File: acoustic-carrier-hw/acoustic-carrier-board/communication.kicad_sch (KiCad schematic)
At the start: 46 parts, among them IC1 ECP5-BGA256, J9 HR911130A, U1 KSZ9031RN, Y1 25MHz

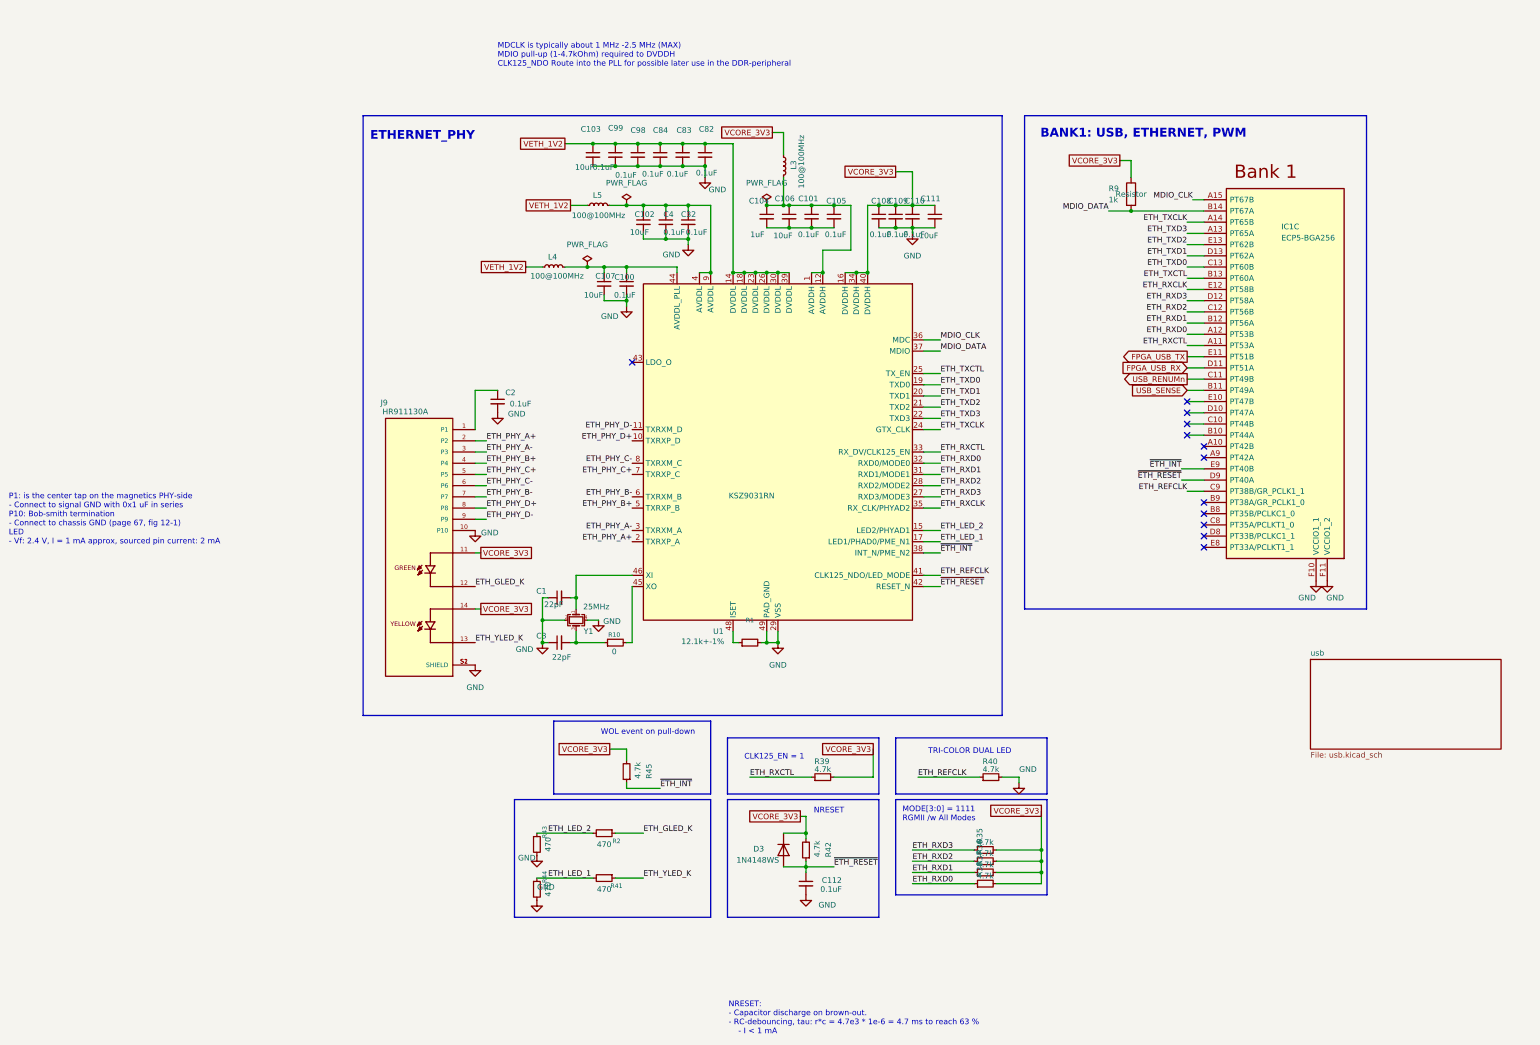
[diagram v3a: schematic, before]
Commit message: [carrier] Checked ethernet decoupling + pins + pad + resonator
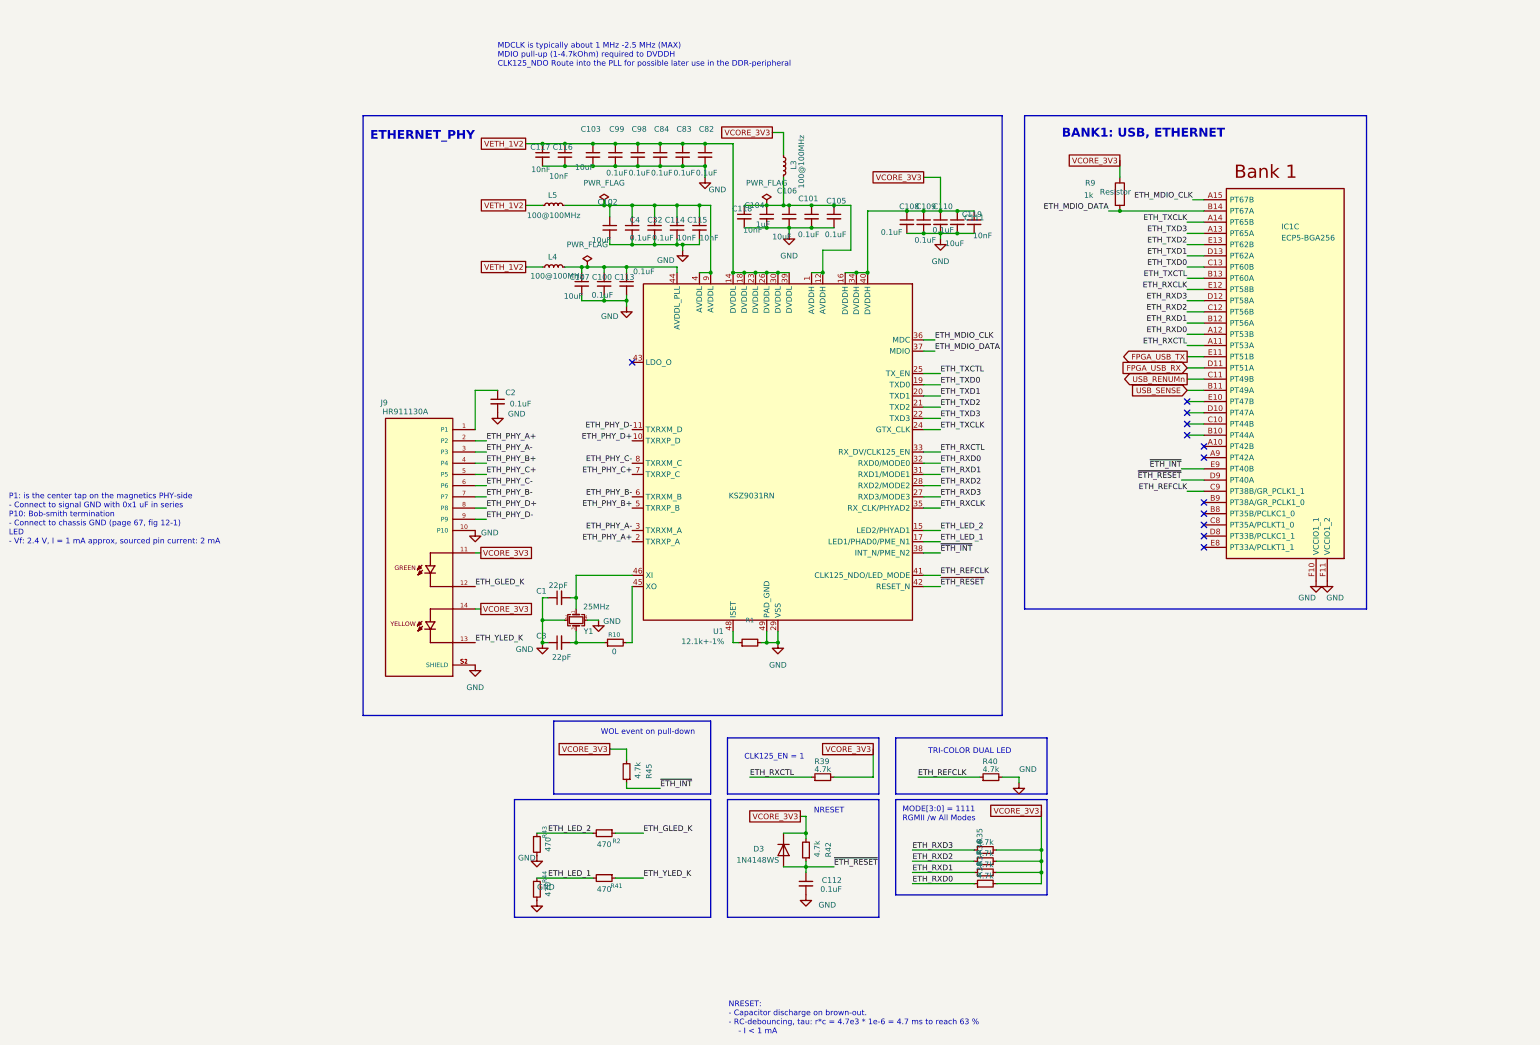
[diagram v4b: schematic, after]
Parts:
- added C113: 0.1uF, Capacitor_SMD:C_0402_1005Metric, symbol Device:C_Small
- added C114, C115, C116, C117, C118, C119: 10nF, Capacitor_SMD:C_0402_1005Metric, symbol Device:C_Small
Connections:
- net GND: now also C101.2, C104.2, C105.2, C106.2, C113.2, C114.2, C115.2, C116.2, C117.2, C118.2, C119.2
- net VCORE_3V3: now also C119.1
- net VETH_1V2: now also C116.1, C117.1
- net at C102.1, C32.1, C4.1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: now also C114.1, C115.1
- net at C100.1, C107.1, L4.1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: now also C113.1
- net at C101.1, C104.1, C105.1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: now also C118.1
- net MDIO_CLK renamed ETH_MDIO_CLK
- net MDIO_DATA renamed ETH_MDIO_DATA
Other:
- removed sheet usb
- note added: "BANK1: USB, ETHERNET"
- note removed: "BANK1: USB, ETHERNET, PWM"
- moved on the sheet: C100, C108, C109, C110, C32, C4, L5, R9

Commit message: [carrier] Checked ethernet phy
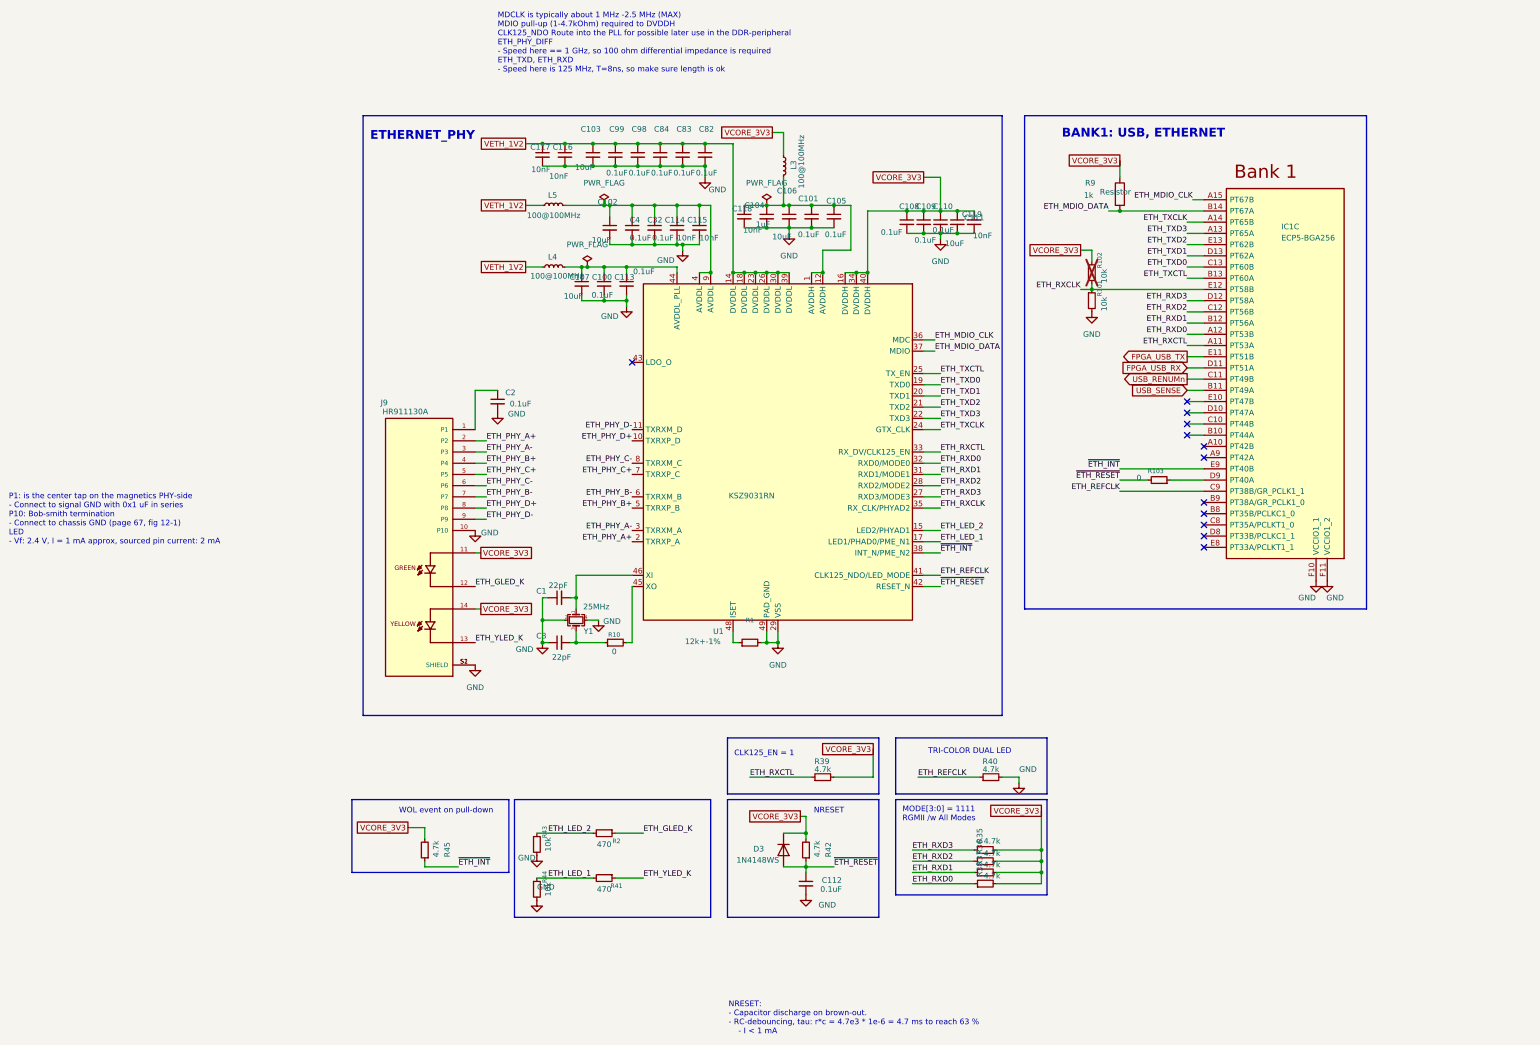
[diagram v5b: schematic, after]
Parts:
- added R101, R102: 10k, Resistor_SMD:R_0603_1608Metric, symbol Device:R_Small
- added R103: 0, Resistor_SMD:R_0603_1608Metric, symbol Device:R_Small
- R1: value 12.1k+-1% -> 12k+-1%
- R43, R44: value 470 -> 10k; LPN C23179 -> C25804; MPN 0603WAF4700T5E -> 0603WAF1002T5E
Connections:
- net ETH_RXCLK: now also R101.1, R102.2
- net GND: now also R101.2
- net VCORE_3V3: now also R102.1
- net ~{ETH_RESET}: now also R103.2; no longer IC1.D9 (PT40A)
- new net: IC1.D9 (PT40A), R103.1
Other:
- note added: "MDCLK is typically about 1 MHz -2.5 MHz (MAX) MDIO pull-up (1-4.7kOhm) required to DVDDH CLK125_NDO Route into the PLL for possible later use in the DDR-peripheral ETH_PHY_DIFF - Speed here == 1 GHz, so 100 ohm differential impedance is required ETH_TXD, ETH_RXD - Speed here is 125 MHz, T=8ns, so make sure length is ok"
- note removed: "MDCLK is typically about 1 MHz -2.5 MHz (MAX) MDIO pull-up (1-4.7kOhm) required to DVDDH CLK125_NDO Route into the PLL for possible later use in the DDR-peripheral"
- moved on the sheet: R45

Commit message: [carrier] Added separate buses for ddr3 ctrl-cmd and dq-groups
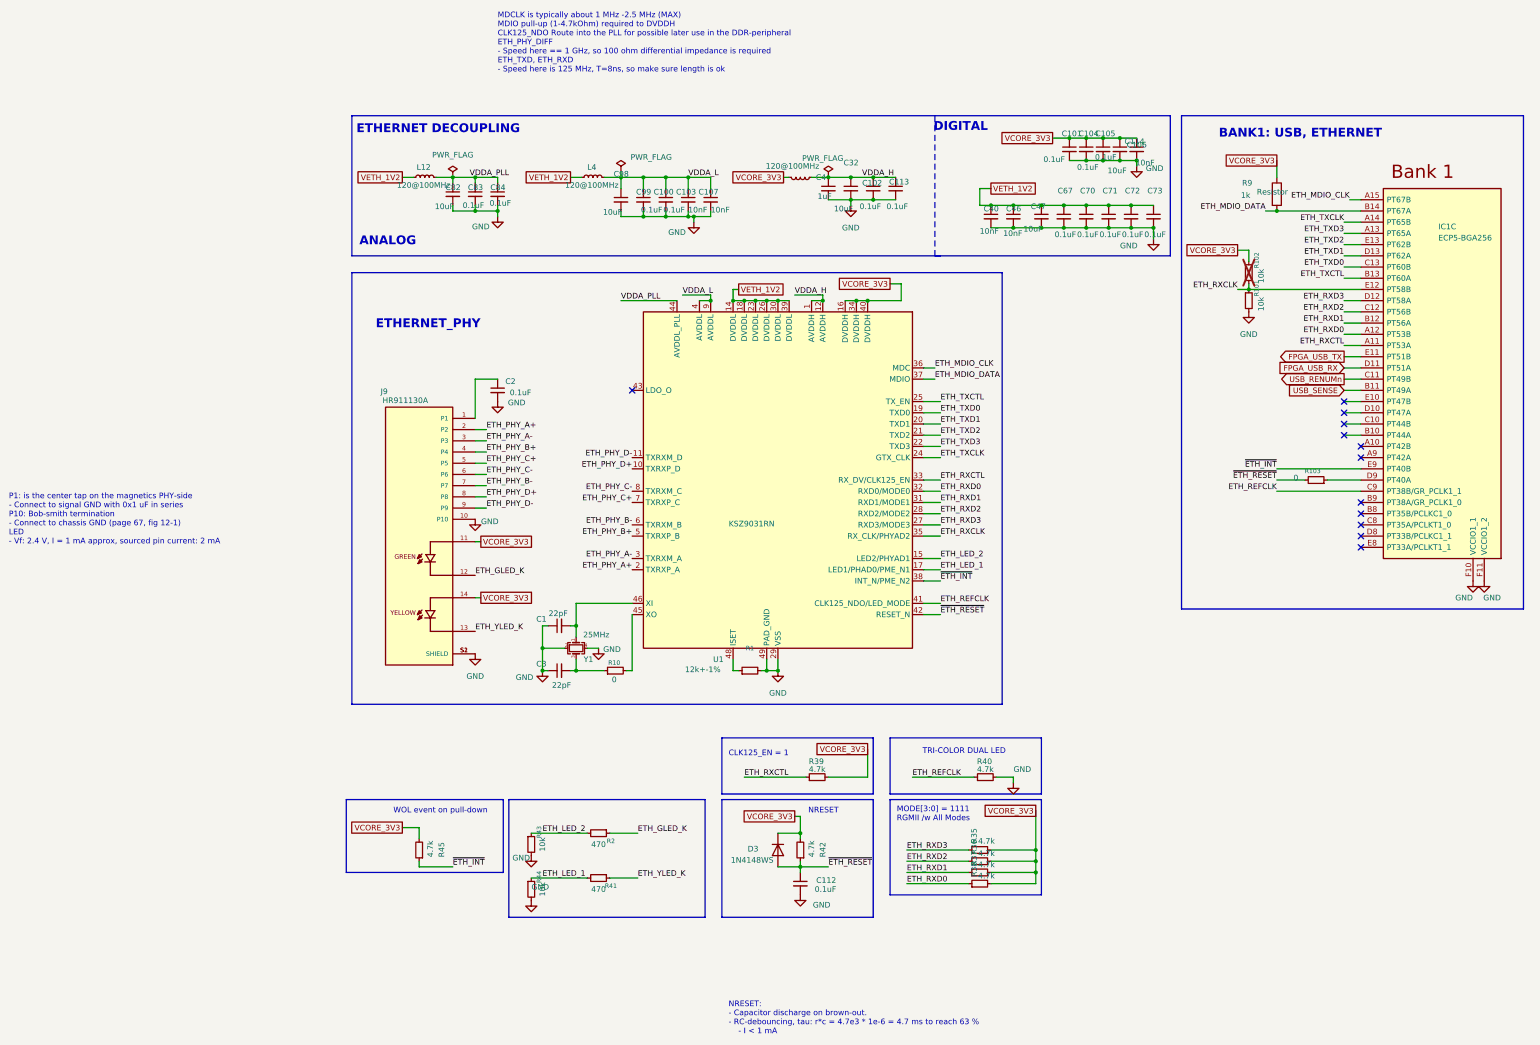
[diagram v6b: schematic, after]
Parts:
- removed C108, C109, C110: 0.1uF, Capacitor_SMD:C_0402_1005Metric, symbol Device:C_Small
- removed C111: 10uF, Capacitor_SMD:C_0603_1608Metric, symbol Device:C_Small
- removed C115, C116, C117, C118, C119: 10nF, Capacitor_SMD:C_0402_1005Metric, symbol Device:C_Small
- removed L3: 100@100MHz, Inductor_SMD:L_0805_2012Metric, symbol Device:L_Small
- added C40, C46: 10nF, Capacitor_SMD:C_0402_1005Metric, symbol Device:C_Small
- added C47: 10uF, Capacitor_SMD:C_0603_1608Metric, symbol Device:C_Small
- added C67, C70, C71, C72, C73: 0.1uF, Capacitor_SMD:C_0402_1005Metric, symbol Device:C_Small
- added L12: 120@100MHz, Inductor_SMD:L_0603_1608Metric, symbol Device:L_Small
- C102: value 10uF -> 0.1uF; footprint Capacitor_SMD:C_0603_1608Metric -> Capacitor_SMD:C_0402_1005Metric; LPN C19702 -> C307331; MPN CL10A106KP8NNNC -> CL05B104KB54PNC
- C103, C107: value 10uF -> 10nF; footprint Capacitor_SMD:C_0603_1608Metric -> Capacitor_SMD:C_0402_1005Metric; LPN C19702 -> C15195; MPN CL10A106KP8NNNC -> CL05B103KB5NNNC
- C104: value 1uF -> 0.1uF; footprint Capacitor_SMD:C_0805_2012Metric -> Capacitor_SMD:C_0402_1005Metric; LPN C28323 -> C307331; MPN CL21B105KBFNNNE -> CL05B104KB54PNC
- C32, C82, C98: value 0.1uF -> 10uF; footprint Capacitor_SMD:C_0402_1005Metric -> Capacitor_SMD:C_0603_1608Metric; LPN C307331 -> C19702; MPN CL05B104KB54PNC -> CL10A106KP8NNNC
- C4: value 0.1uF -> 1uF; footprint Capacitor_SMD:C_0402_1005Metric -> Capacitor_SMD:C_0805_2012Metric; LPN C307331 -> C28323; MPN CL05B104KB54PNC -> CL21B105KBFNNNE
- L4, L5: value 100@100MHz -> 120@100MHz; footprint Inductor_SMD:L_0805_2012Metric -> Inductor_SMD:L_0603_1608Metric; LPN C1015 -> C113030; MPN GZ2012D101TF -> BLM18SG121TN1D
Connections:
- net GND: now also C40.2, C46.2, C47.2, C67.2, C70.2, C71.2, C72.2, C73.2
- net VCORE_3V3: now also C101.1, C104.1, C105.1, C106.1, C114.1, L5.1
- net VETH_1V2: now also C40.1, C46.1, C47.1, C67.1, C70.1, C71.1, C72.1, C73.1, L12.2; no longer C103.1, C82.1, C83.1, C84.1, C98.1, C99.1, L5.2
- net VDDA_L: now reaches C100.1, C107.1, L4.1
- net VDDA_L: now also C103.1, C98.1, C99.1, U1.4 (AVDDL), U1.9 (AVDDL); no longer C113.1, U1.44 (AVDDL_PLL)
- new net VDDA_H: C102.1, C113.1, C32.1, C4.1, L5.2, U1.1 (AVDDH), U1.12 (AVDDH)
- new net VDDA_PLL: C82.1, C83.1, C84.1, L12.1, U1.44 (AVDDL_PLL)
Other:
- note added: "ANALOG"
- note added: "DIGITAL"
- note added: "ETHERNET DECOUPLING"
- moved on the sheet: C1, C112, C2, C3, D3, IC1C, J9, R1, R10, R101, R102, R103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

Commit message: [carrier] Worked on USB connector
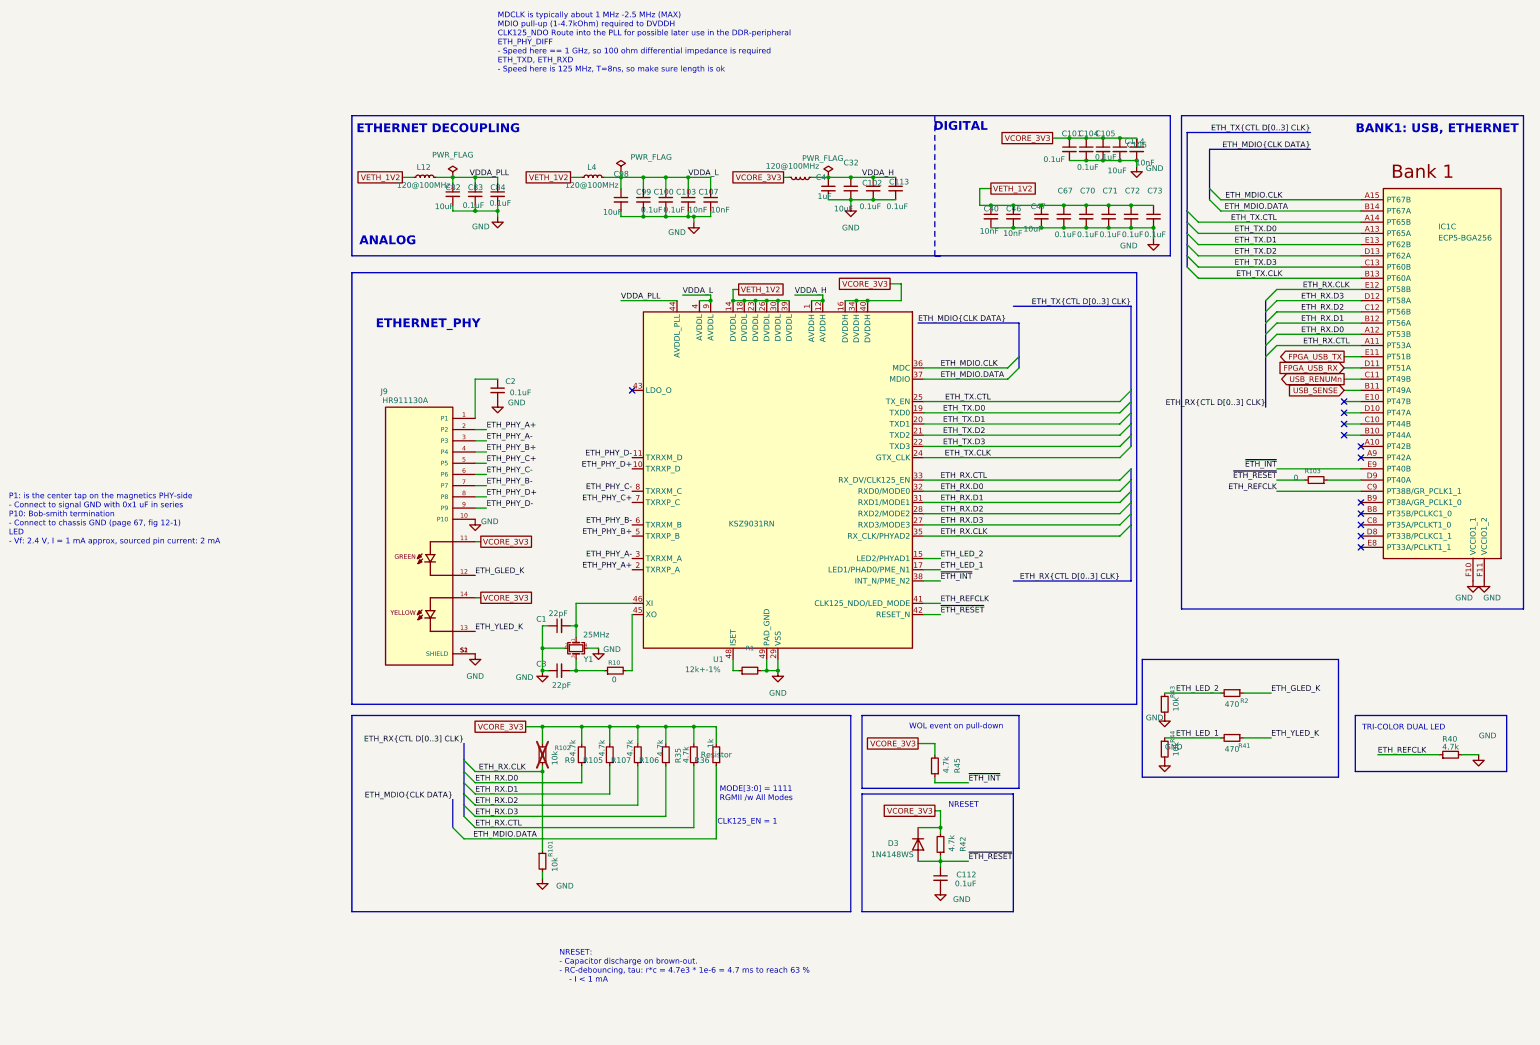
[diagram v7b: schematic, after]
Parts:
- removed R37, R38, R39: 4.7k, Resistor_SMD:R_0402_1005Metric, symbol Device:R_Small
- removed R9: 1k, Resistor_SMD:R_0805_2012Metric_Pad1.20x1.40mm_HandSolder, symbol Device:R
- added R105, R106, R107, R9: 4.7k, Resistor_SMD:R_0402_1005Metric, symbol Device:R_Small
- R36: value 4.7k -> 1k; footprint Resistor_SMD:R_0402_1005Metric -> Resistor_SMD:R_0805_2012Metric_Pad1.20x1.40mm_HandSolder; LPN 0402WGF4701TCE -> C17513; MPN C25900 -> 0805W8F1001T5E
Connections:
- net VCORE_3V3: now also R105.2, R106.2, R107.2, R9.2
- net ETH_MDIO_CLK renamed ETH_MDIO.CLK
- net ETH_MDIO_DATA renamed ETH_MDIO.DATA
- net ETH_MDIO.DATA: now also R36.1
- net ETH_RXCLK renamed ETH_RX.CLK
- net ETH_RXCTL renamed ETH_RX.CTL
- net ETH_RX.CTL: now also R35.1
- net ETH_RXD0 renamed ETH_RX.D0
- net ETH_RX.D0: now also R9.1
- net ETH_RXD1 renamed ETH_RX.D1
- net ETH_RX.D1: now also R105.1
- net ETH_RXD2 renamed ETH_RX.D2
- net ETH_RX.D2: now also R107.1; no longer R36.1
- net ETH_RXD3 renamed ETH_RX.D3
- net ETH_RX.D3: now also R106.1; no longer R35.1
- net ETH_TXCLK renamed ETH_TX.CLK
- net ETH_TX.CLK: now also IC1.B13 (PT60A); no longer IC1.A14 (PT65B)
- net ETH_TXCTL renamed ETH_TX.CTL
- net ETH_TX.CTL: now also IC1.A14 (PT65B); no longer IC1.B13 (PT60A)
- net ETH_TXD0 renamed ETH_TX.D0
- net ETH_TX.D0: now also IC1.A13 (PT65A); no longer IC1.C13 (PT60B)
- net ETH_TXD1 renamed ETH_TX.D1
- net ETH_TX.D1: now also IC1.E13 (PT62B); no longer IC1.D13 (PT62A)
- net ETH_TXD2 renamed ETH_TX.D2
- net ETH_TX.D2: now also IC1.D13 (PT62A); no longer IC1.E13 (PT62B)
- net ETH_TXD3 renamed ETH_TX.D3
- net ETH_TX.D3: now also IC1.C13 (PT60B); no longer IC1.A13 (PT65A)
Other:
- moved on the sheet: C112, D3, R101, R102, R2, R40, R41, R42, R43, R44, R45
